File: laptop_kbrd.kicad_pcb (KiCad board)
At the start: 2 copper layers, 141.3 x 42.1 mm, 125 parts, among them CON1 AVR-ISP-6-DR, CON2 AVR-ISP-6-DR, CON3 AVR-ISP-6-DR, K1 CASE_OPEN, K2 CASE_OPEN, Q1 MOSFET_N, Q10 MOSFET_N, Q11 MOSFET_N, Q2 MOSFET_N, Q3 MOSFET_N, Q4 MOSFET_N, Q5 MOSFET_N, Q6 MOSFET_N, Q7 MOSFET_N, Q8 ALS_PT19, Q9 MOSFET_N, SW1 MCU_RST, SW2 BT_ASSCN, SW3 POWER, SW4 CASE_PUSH, SW5 MCU_RST, SW6 MCU_RST, SW7 SPST, U1 ATMEGA32U4-AU, U10 NHD-0440AZ-FL-YBW, U11 NRF24L01+, U12 ATAES132A, U13 AT97SC3205T, U14 TUSB2046BVFR, U15 MAX6749, U16 BME280, U17 TPS2041B, U18 LVDS_HEADER, U2 RT9706, U3 ATMEGA32U4, U4 0WX4JF, U5 XF2M-3015-1A, U6 ATMEGA32U4, U7 USB_CAM, U8 EPAPER_V2, U9 USB_A_FEMALE, X1 XTAL 16MHz, X2 XTAL 16MHz, X3 XTAL 16MHz, X4 6MHz

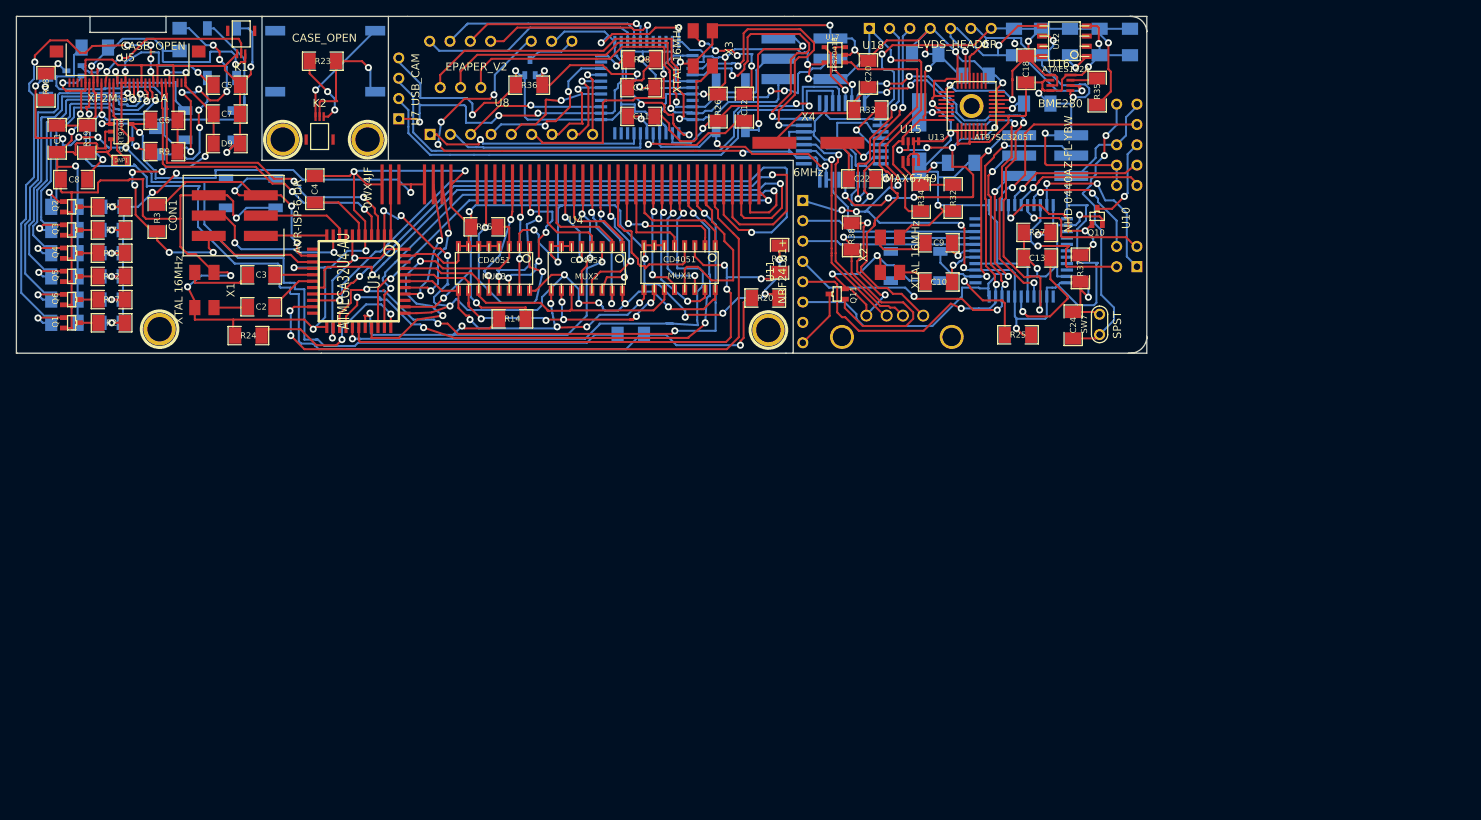
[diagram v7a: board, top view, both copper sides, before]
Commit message: Changed internal Edge cuts to Silkscreen double lines for cutting with fret saw later. Generated and zipped Gerber files and drill file. Tested with Oshpark.
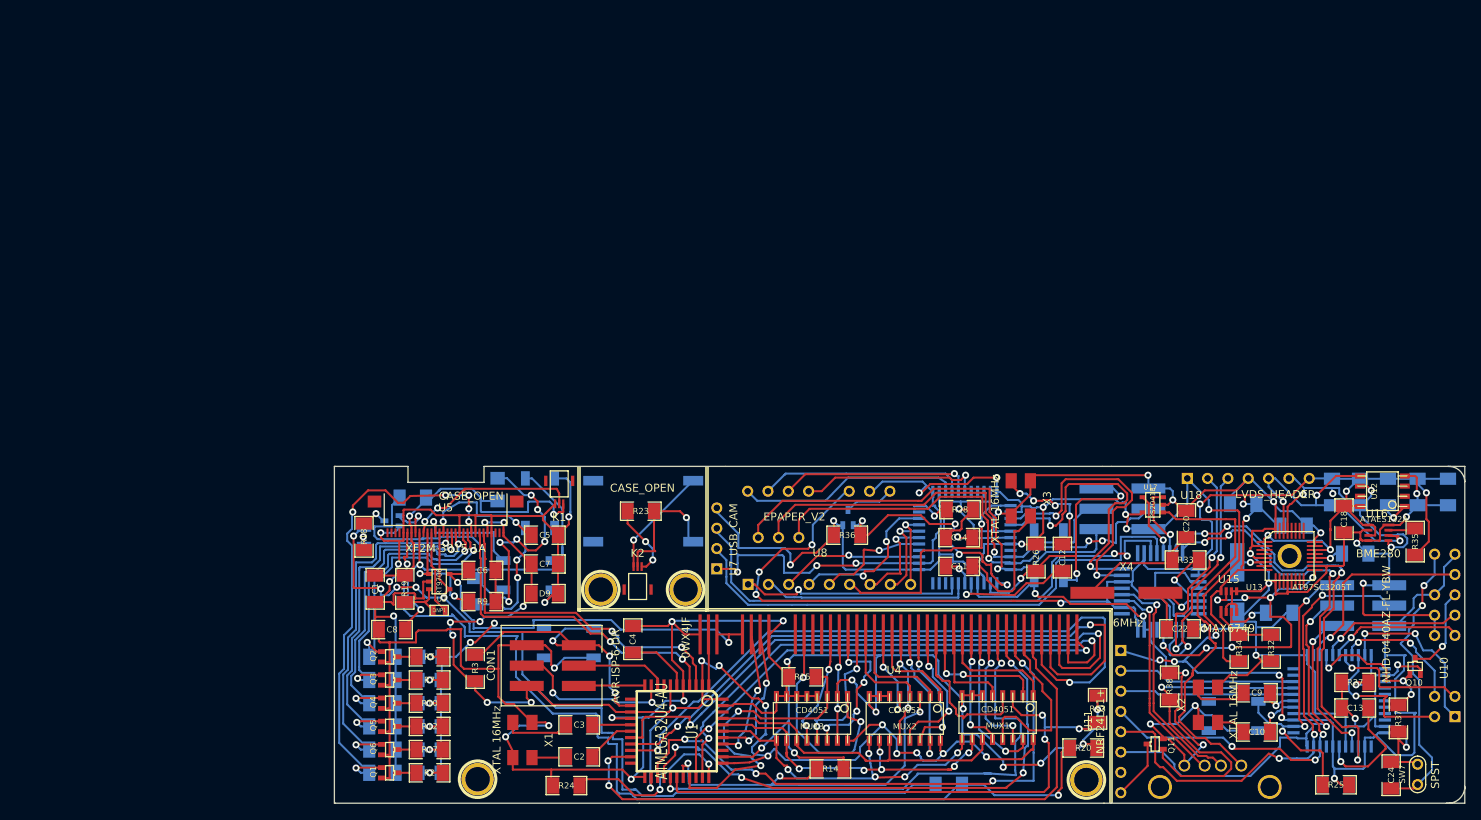
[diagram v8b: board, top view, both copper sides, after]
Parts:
- moved D2 68.9 mm to (147.1, 143.2)
- moved R1 68.9 mm to (141.1, 157.8)
- moved R16 68.9 mm to (141.1, 154.8)
- moved R24 68.9 mm to (164.1, 159.3)
- moved R4 68.9 mm to (141.1, 143.2)
- moved R6 68.9 mm to (141.1, 146.2)
- moved R8 68.9 mm to (141.1, 149.1)
- moved R9 68.9 mm to (153.6, 136.3)
- moved U10 68.9 mm to (273.9, 141.8)
- moved X1 68.9 mm to (158.6, 153.7)
- moved ? 68.9 mm to (229.1, 158.7)
- moved ? 68.9 mm to (152.9, 158.6)
- moved ? 68.9 mm to (168.3, 134.8)
- moved ? 68.9 mm to (178.9, 134.8)
- moved C1 68.9 mm to (140.2, 134.8)
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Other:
- outline, holes or cut-outs redrawn
